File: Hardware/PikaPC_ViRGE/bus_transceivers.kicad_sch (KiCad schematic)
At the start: 14 parts, among them U10 74LS573, U12 74FCT2245, U13 74FCT2245, U14 74FCT2245, U15 74FCT2245, U8 74LS573, U9 74LS573

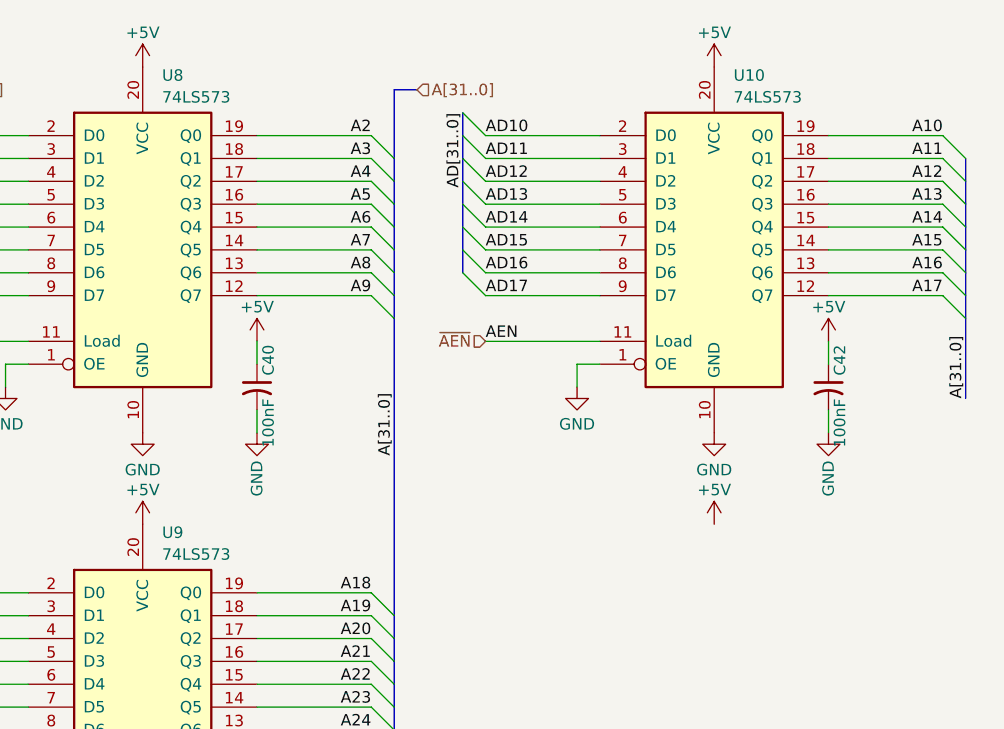
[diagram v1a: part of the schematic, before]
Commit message: ViRGE card PCB layout
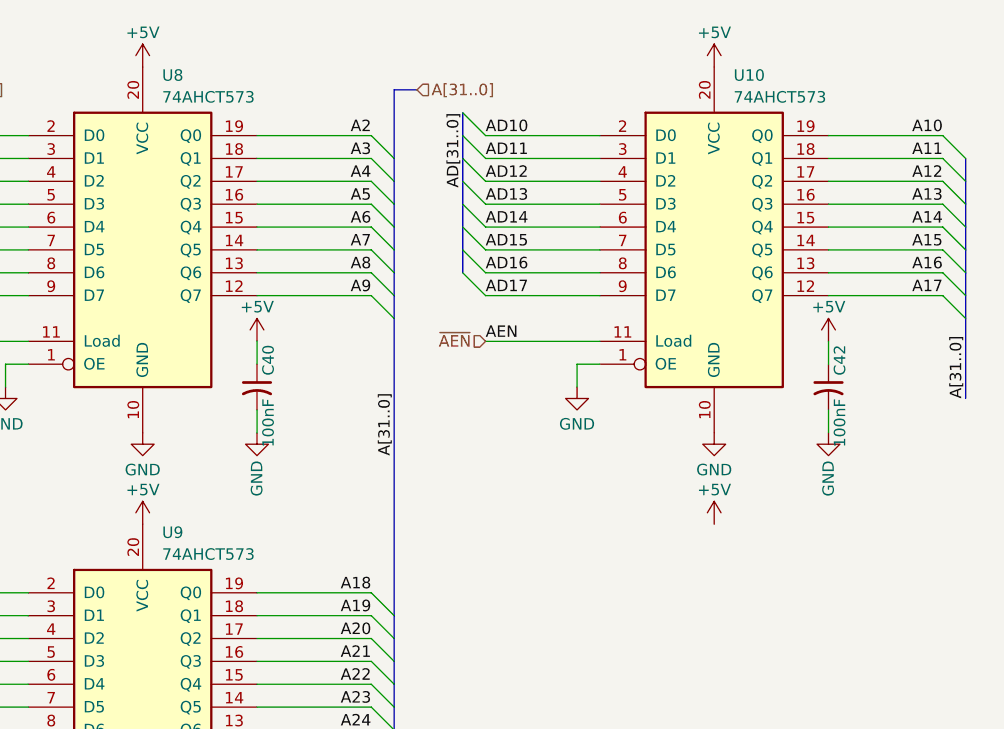
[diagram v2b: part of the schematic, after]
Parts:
- U10, U8, U9: value 74LS573 -> 74AHCT573
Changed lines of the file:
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@@
 			)
 		)
-		(property "Value" "74LS573"
+		(property "Value" "74AHCT573"
 			(at 47.8633 74.4798 0)
 			(effects
@@
 			)
 		)
-		(property "Value" "74LS573"
+		(property "Value" "74AHCT573"
 			(at 111.3633 23.6798 0)
 			(effects
@@
 			)
 		)
-		(property "Value" "74LS573"
+		(property "Value" "74AHCT573"
 			(at 47.8633 23.6798 0)
 			(effects

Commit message: Prep for output
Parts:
- C40, C41, C42, C44, C45, C46, C47: Mouser (none) -> 187-CL21B104KACNNNC
- U12, U13, U14, U15: Mouser (none) -> 595-CY74FCT2245TSOCT
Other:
- note added: "These address latches probably aren't necessary, because ViRGE is supposed to latch the address bus one clock after ~{ADS}."
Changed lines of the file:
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@@
 	(generator_version "9.0")
 	(paper "A")
+	(text "These address latches probably\naren't necessary, because ViRGE\nis supposed to latch the address\nbus one clock after ~{ADS}. "
+		(exclude_from_sim no)
+		(at 88.9 76.2 0)
+		(effects
+			(font
+				(size 1.27 1.27)
+			)
+			(justify left top)
+		)
+	)
 	(bus_entry
 		(at 208.28 78.74)
@@
 			)
 		)
+		(property "Mouser" "187-CL21B104KACNNNC"
+			(at 58.42 55.88 90)
+			(effects
+				(font
+					(size 1.27 1.27)
+				)
+				(hide yes)
+			)
+		)
 		(pin "2"
 		)
@@
 			)
 		)
+		(property "Mouser" "187-CL21B104KACNNNC"
+			(at 185.42 55.88 90)
+			(effects
+				(font
+					(size 1.27 1.27)
+				)
+				(hide yes)
+			)
+		)
 		(pin "2"
 		)
@@
 			)
 		)
+		(property "Mouser" "595-CY74FCT2245TSOCT "
+			(at 236.22 40.64 0)
+			(effects
+				(font
+					(size 1.27 1.27)
+				)
+				(hide yes)
+			)
+		)
 		(pin "8"
 		)
@@
 			)
 		)
+		(property "Mouser" "595-CY74FCT2245TSOCT "
+			(at 172.72 91.44 0)
+			(effects
+				(font
+					(size 1.27 1.27)
+				)
+				(hide yes)
+			)
+		)
 		(pin "8"
 		)
@@
 			)
 		)
+		(property "Mouser" "187-CL21B104KACNNNC"
+			(at 58.42 106.68 90)
+			(effects
+				(font
+					(size 1.27 1.27)
+				)
+				(hide yes)
+			)
+		)
 		(pin "2"
 		)
@@
 			)
 		)
+		(property "Mouser" "187-CL21B104KACNNNC"
+			(at 248.92 55.88 90)
+			(effects
+				(font
+					(size 1.27 1.27)
+				)
+				(hide yes)
+			)
+		)
 		(pin "2"
 		)
@@
 			)
 		)
+		(property "Mouser" "595-CY74FCT2245TSOCT "
+			(at 236.22 91.44 0)
+			(effects
+				(font
+					(size 1.27 1.27)
+				)
+				(hide yes)
+			)
+		)
 		(pin "8"
 		)
@@
 	)
 	(symbol
-		(lib_id "power:+5V")
-		(at 109.22 71.12 0)
-		(unit 1)
-		(exclude_from_sim no)
-		(in_bom yes)
-		(on_board yes)
-		(dnp no)
-		(property "Reference" "#PWR0147"
-			(at 109.22 74.93 0)
-			(effects
-				(font
-					(size 1.27 1.27)
-				)
-				(hide yes)
-			)
-		)
-		(property "Value" "+5V"
-			(at 109.22 67.31 0)
-			(effects
-				(font
-					(size 1.27 1.27)
-				)
-			)
-		)
-		(property "Footprint" ""
-			(at 109.22 71.12 0)
-			(effects
-				(font
-					(size 1.27 1.27)
-				)
-				(hide yes)
-			)
-		)
-		(property "Datasheet" ""
-			(at 109.22 71.12 0)
-			(effects
-				(font
-					(size 1.27 1.27)
-				)
-				(hide yes)
-			)
-		)
-		(property "Description" "Power symbol creates a global label with name \"+5V\""
-			(at 109.22 71.12 0)
-			(effects
-				(font
-					(size 1.27 1.27)
-				)
-				(hide yes)
-			)
-		)
-		(pin "1"
-		)
-		(instances
-			(project "PikaPC_ViRGE"
-				(path "/dd18a86c-f3c8-46f4-a73e-5b02d2ebb148/b87e7203-ea3a-46a7-9e06-4b89d81b9033/5b9289f9-33c5-4aee-a588-cd93e23243f9"
-					(reference "#PWR0147")
-					(unit 1)
-				)
-			)
-		)
-	)
-	(symbol
 		(lib_id "Device:C_Small_US")
 		(at 248.92 106.68 0)
@@
 			)
 		)
+		(property "Mouser" "187-CL21B104KACNNNC"
+			(at 248.92 106.68 90)
+			(effects
+				(font
+					(size 1.27 1.27)
+				)
+				(hide yes)
+			)
+		)
 		(pin "2"
 		)
@@
 			)
 		)
+		(property "Mouser" "187-CL21B104KACNNNC"
+			(at 121.92 55.88 90)
+			(effects
+				(font
+					(size 1.27 1.27)
+				)
+				(hide yes)
+			)
+		)
 		(pin "2"
 		)
@@
 			)
 		)
+		(property "Mouser" "595-CY74FCT2245TSOCT "
+			(at 172.72 40.64 0)
+			(effects
+				(font
+					(size 1.27 1.27)
+				)
+				(hide yes)
+			)
+		)
 		(pin "8"
 		)
@@
 			(effects
 				(font
+					(size 1.27 1.27)
+				)
+				(hide yes)
+			)
+		)
+		(property "Mouser" "187-CL21B104KACNNNC"
+			(at 185.42 106.68 90)
+			(effects
+				(font
